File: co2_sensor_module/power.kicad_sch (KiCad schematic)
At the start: 7 parts, among them U3 TPS62125DSG

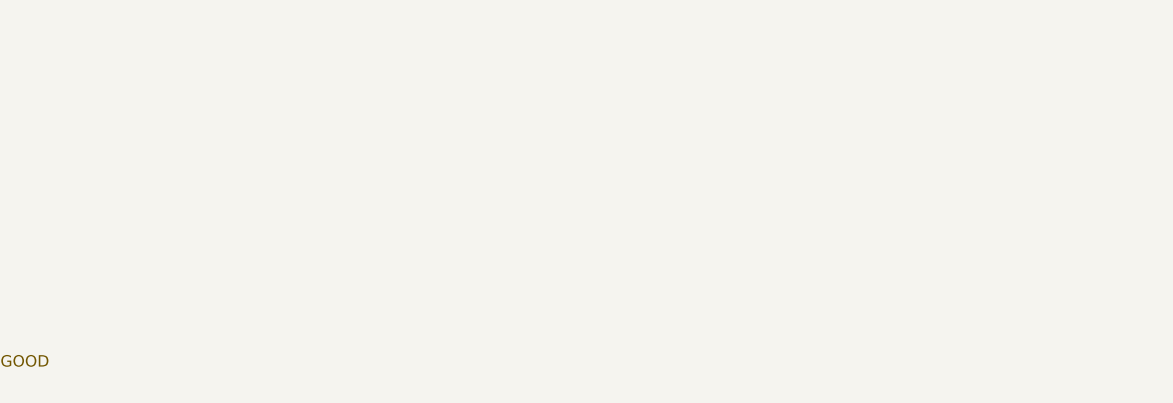
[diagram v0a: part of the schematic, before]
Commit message: mostly done w/ sensor module
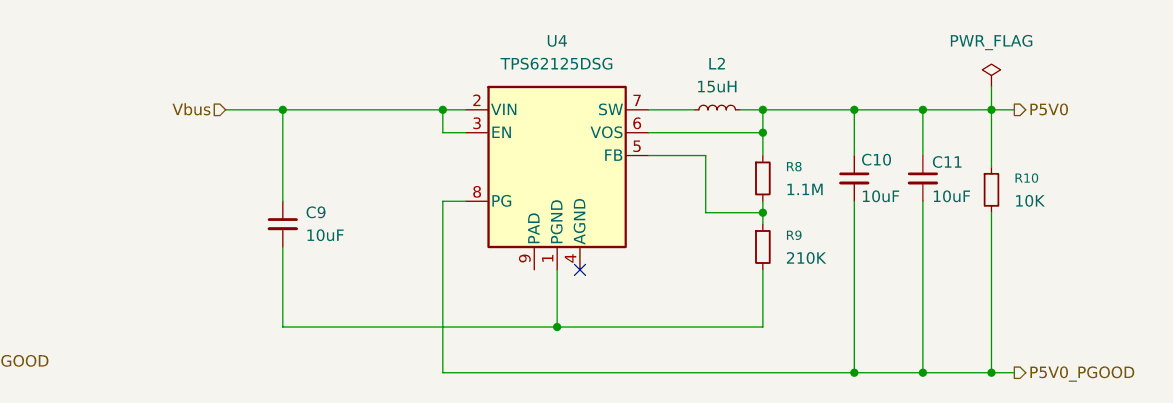
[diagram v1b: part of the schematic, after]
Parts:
- added C10, C11, C9: 10uF, Capacitor_SMD:C_0805_2012Metric, symbol Device:C_Small
- added L2: 15uH, Inductor_SMD:L_1008_2520Metric, symbol Device:L_Small
- added R10: 10K, Resistor_SMD:R_0402_1005Metric, symbol Device:R_Small
- added R8: 1.1M, Resistor_SMD:R_0402_1005Metric, symbol Device:R_Small
- added R9: 210K, Resistor_SMD:R_0402_1005Metric, symbol Device:R_Small
- added U4: TPS62125DSG, Package_SON:Texas_DSG0008A_WSON-8-1EP_2x2mm_P0.5mm_EP0.9x1.6mm_ThermalVias, symbol Regulator_Switching:TPS62125DSG
- C7, C8: footprint (none) -> Capacitor_SMD:C_0805_2012Metric; LCSC (none) -> C15850
- L1: footprint (none) -> Inductor_SMD:L_1008_2520Metric; LCSC (none) -> C5832376
- R5, R6: footprint (none) -> Resistor_SMD:R_0402_1005Metric; LCSC (none) -> C2933079
- R7: footprint (none) -> Resistor_SMD:R_0402_1005Metric; LCSC (none) -> C25744
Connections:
- net Vbus: now also C9.1, U4.2 (VIN), U4.3 (EN)
- new net: R8.2, R9.1, U4.5 (FB)
- new net: C9.2, R9.2, U4.1 (PGND)
- new net: L2.1, U4.7 (SW)
- new net P5V0: C10.1, C11.1, L2.2, R10.1, R8.1, U4.6 (VOS)
- new net P5V0_PGOOD: C10.2, C11.2, R10.2, U4.8 (PG)
- no-connect marks 1 -> 2

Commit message: first draft of sensor schematic is done!
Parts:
- removed R10, R7: 10K, Resistor_SMD:R_0402_1005Metric, symbol Device:R_Small
- removed U3: TPS62125DSG, Package_SON:Texas_DSG0008A_WSON-8-1EP_2x2mm_P0.5mm_EP0.9x1.6mm_ThermalVias, symbol Regulator_Switching:TPS62125DSG
- added R21, R26: 100K, Capacitor_SMD:C_0402_1005Metric, symbol Device:R_Small
- added U10: TPS62125DSG, Package_SON:Texas_DSG0008A_WSON-8-1EP_2x2mm_P0.5mm_EP0.9x1.6mm_ThermalVias, symbol Regulator_Switching:TPS62125DSG
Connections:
- net P3V3: now also R21.1, U10.6 (VOS)
- net P3V3_PGOOD: now also R21.2, U10.8 (PG)
- net P5V0: now also R26.1
- net P5V0_PGOOD: now also R26.2; no longer C10.2, C11.2
- net Vbus: now also U10.2 (VIN), U10.3 (EN)
- net GND: now reaches C7.2, C8.2, R6.2
- net GND: now also C10.2, C11.2, C9.2, R9.2, U4.1 (PGND), U4.9 (PAD), U10.1 (PGND), U10.9 (PAD)
- net at R5.2, R6.1: now also U10.5 (FB)
- net at L1.1: now also U10.7 (SW)
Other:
- note added: "PG is open drain"

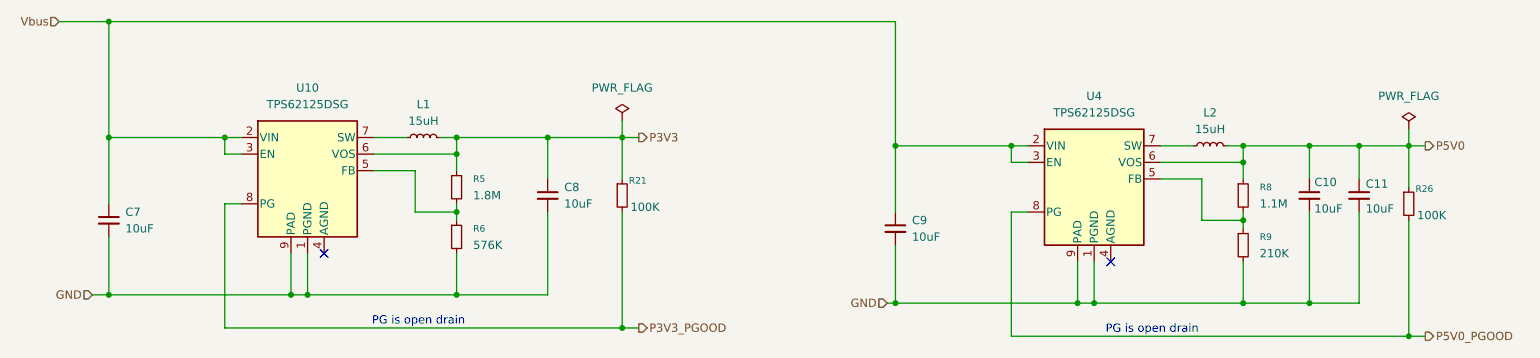
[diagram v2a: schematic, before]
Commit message: mostly done with sensor module
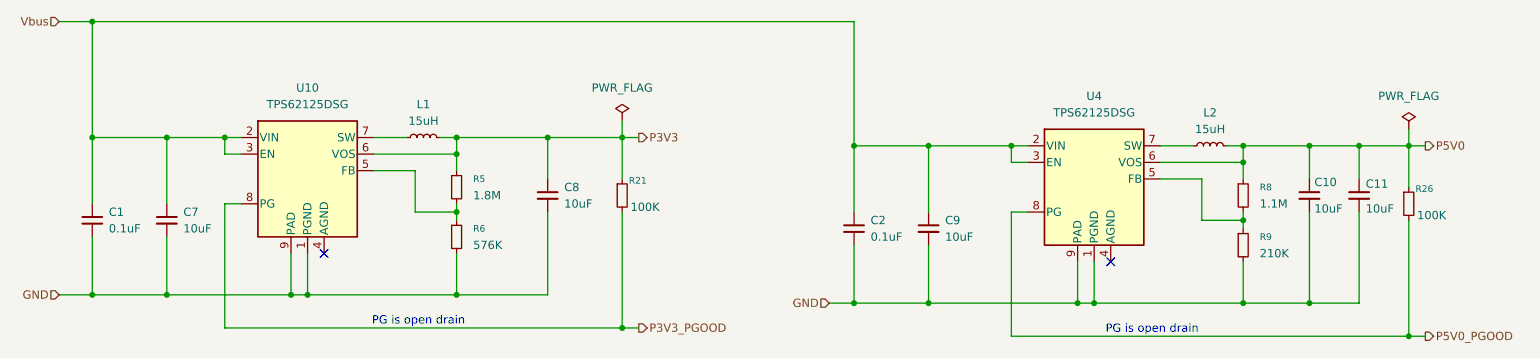
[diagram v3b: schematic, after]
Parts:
- added C1, C2: 0.1uF, Capacitor_SMD:C_0603_1608Metric, symbol Device:C_Small
- R6: LCSC C2933079 -> C2085028
- U10, U4: footprint Package_SON:Texas_DSG0008A_WSON-8-1EP_2x2mm_P0.5mm_EP0.9x1.6mm_ThermalVias -> Package_SON:Texas_DSG0008A_WSON-8-1EP_2x2mm_P0.5mm_EP0.9x1.6mm
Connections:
- net GND: now also C1.2, C2.2
- net Vbus: now also C1.1, C2.1
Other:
- moved on the sheet: C7
